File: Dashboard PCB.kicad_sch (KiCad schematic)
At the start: 38 parts

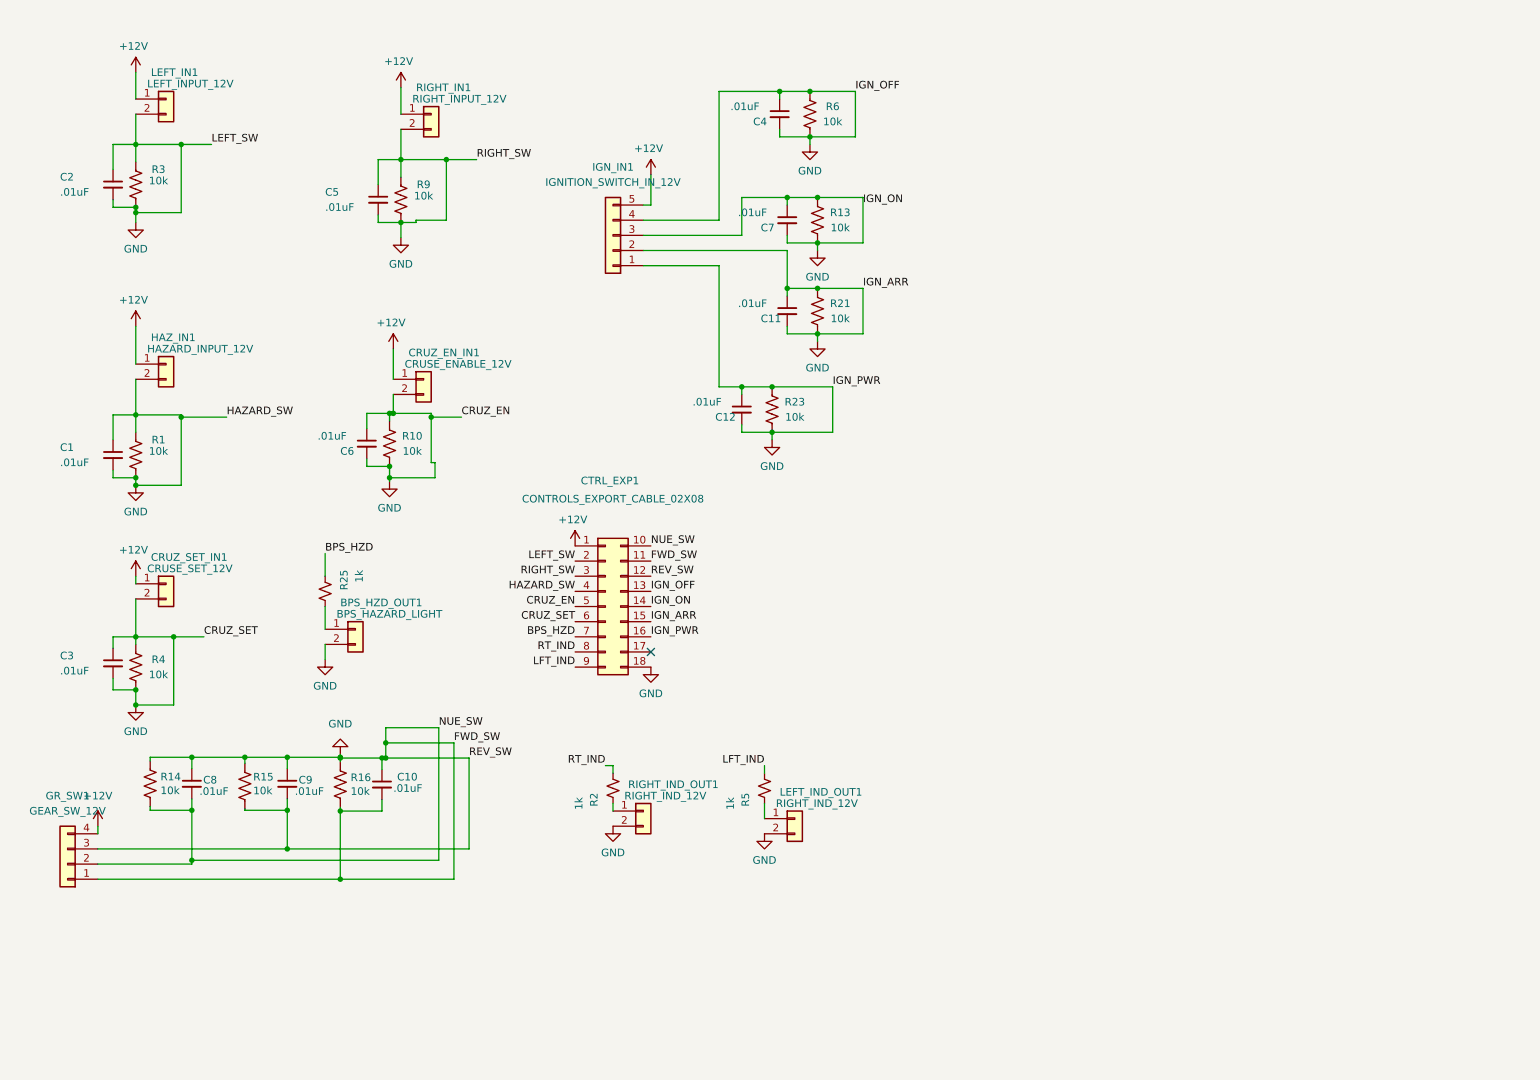
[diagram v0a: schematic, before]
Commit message: Ready for review I think :+1:
Switched design from modular to big board :). Plz rev schem thaks :P
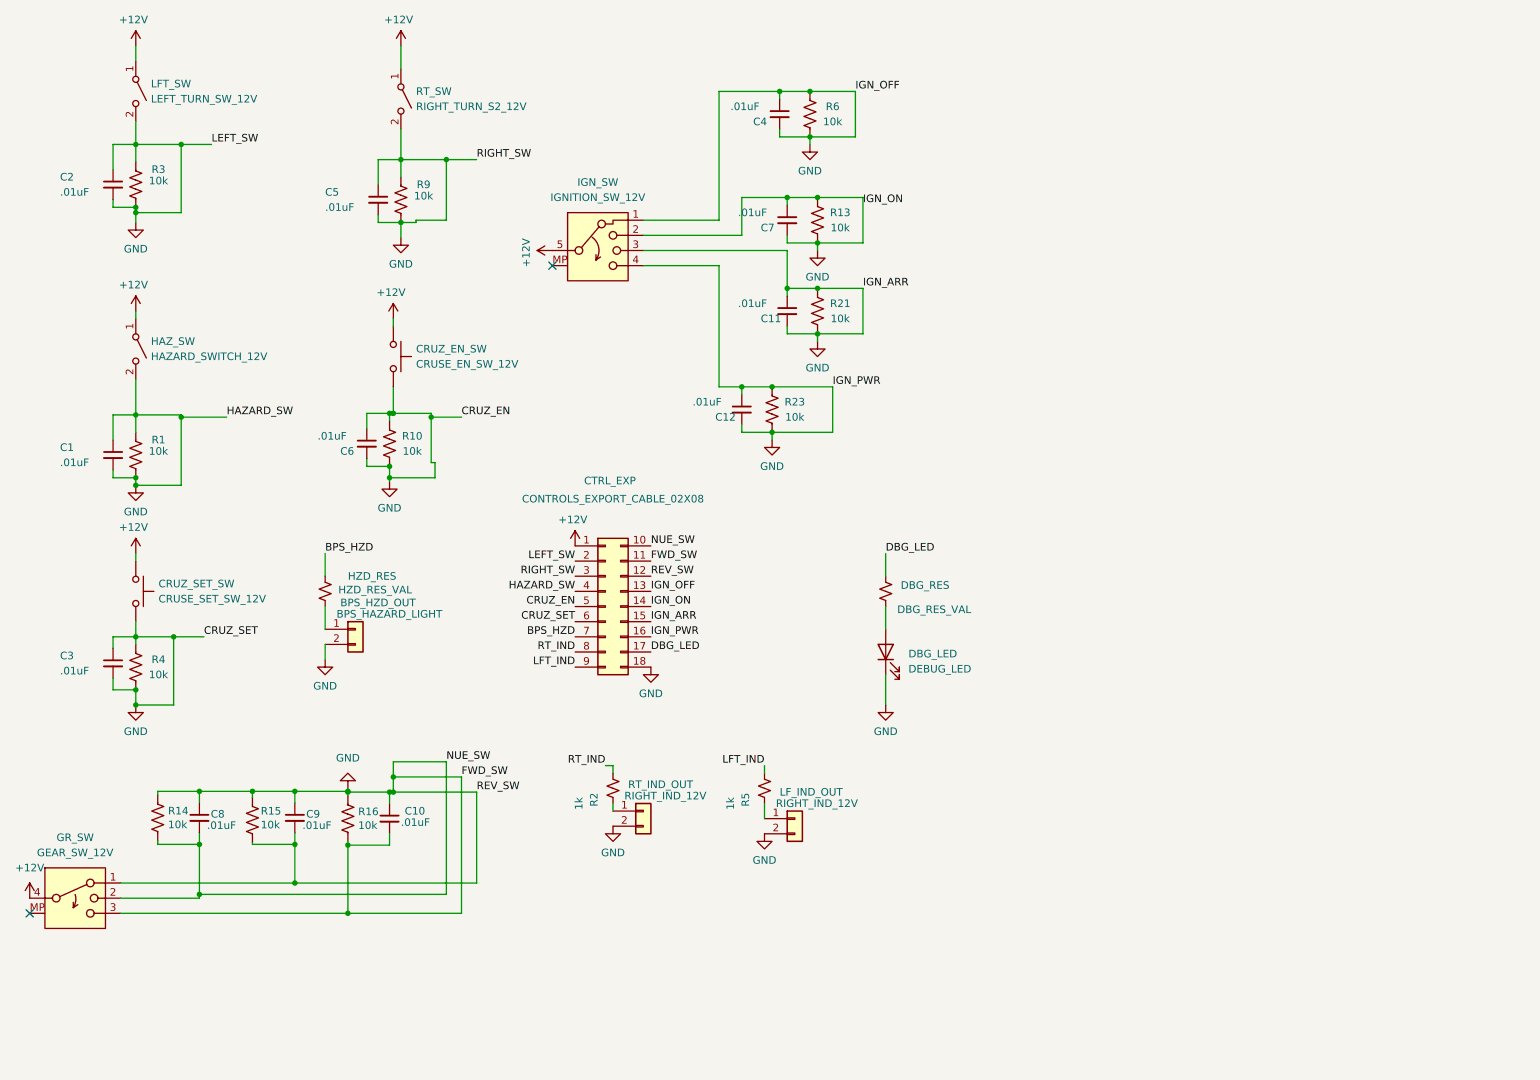
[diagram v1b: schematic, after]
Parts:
- removed CRUZ_EN_IN1: CRUSE_ENABLE_12V, Connector_Molex:Molex_Micro-Fit_3.0_43650-0215_1x02_P3.00mm_Vertical, symbol Connector_Generic:Conn_01x02
- removed CRUZ_SET_IN1: CRUSE_SET_12V, Connector_Molex:Molex_Micro-Fit_3.0_43650-0215_1x02_P3.00mm_Vertical, symbol Connector_Generic:Conn_01x02
- removed GR_SW1: GEAR_SW_12V, symbol Connector_Generic:Conn_01x04
- removed HAZ_IN1: HAZARD_INPUT_12V, Connector_Molex:Molex_Micro-Fit_3.0_43650-0215_1x02_P3.00mm_Vertical, symbol Connector_Generic:Conn_01x02
- removed IGN_IN1: IGNITION_SWITCH_IN_12V, symbol Connector_Generic:Conn_01x05
- removed LEFT_IN1: LEFT_INPUT_12V, Connector_Molex:Molex_Micro-Fit_3.0_43650-0215_1x02_P3.00mm_Vertical, symbol Connector_Generic:Conn_01x02
- removed RIGHT_IN1: RIGHT_INPUT_12V, Connector_Molex:Molex_Micro-Fit_3.0_43650-0215_1x02_P3.00mm_Vertical, symbol Connector_Generic:Conn_01x02
- added CRUZ_EN_SW: CRUSE_EN_SW_12V, symbol Switch:SW_Push
- added CRUZ_SET_SW: CRUSE_SET_SW_12V, symbol Switch:SW_Push
- added DBG_LED: DEBUG_LED, symbol Device:LED
- added DBG_RES: DBG_RES_VAL, Resistor_SMD:R_0805_2012Metric, symbol Device:R_Small_US
- added GR_SW: GEAR_SW_12V, symbol Switch:SW_Rotary_1x3_MP
- added HAZ_SW: HAZARD_SWITCH_12V, symbol Switch:SW_SPST
- added IGN_SW: IGNITION_SW_12V, symbol Switch:SW_Rotary_1x4_MP
- added LFT_SW: LEFT_TURN_SW_12V, symbol Switch:SW_SPST
- added RT_SW: RIGHT_TURN_S2_12V, symbol Switch:SW_SPST
- HZD_RES: renamed from R25; value 1k -> HZD_RES_VAL
- renumbered BPS_HZD_OUT1 to BPS_HZD_OUT, CTRL_EXP1 to CTRL_EXP, LEFT_IND_OUT1 to LF_IND_OUT, RIGHT_IND_OUT1 to RT_IND_OUT
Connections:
- net +12V: now also CRUZ_EN_SW.1, CRUZ_SET_SW.1, GR_SW.4, HAZ_SW.1 (A), IGN_SW.5, LFT_SW.1 (A), RT_SW.1 (A)
- net GND: now also CRUZ_EN_SW.2, CRUZ_SET_SW.2, DBG_LED.1 (K), GR_SW.1, GR_SW.2, GR_SW.3, HAZ_SW.2 (B), IGN_SW.1, IGN_SW.2, IGN_SW.3, IGN_SW.4, LFT_SW.2 (B), RT_SW.2 (B)
- net DBG_LED: now reaches CTRL_EXP.17 (Pin_17)
- net DBG_LED: now also DBG_RES.1
- new net: DBG_LED.2 (A), DBG_RES.2
- no-connect marks 1 -> 2
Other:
- moved on the sheet: C10, C8, C9, R14, R15, R16

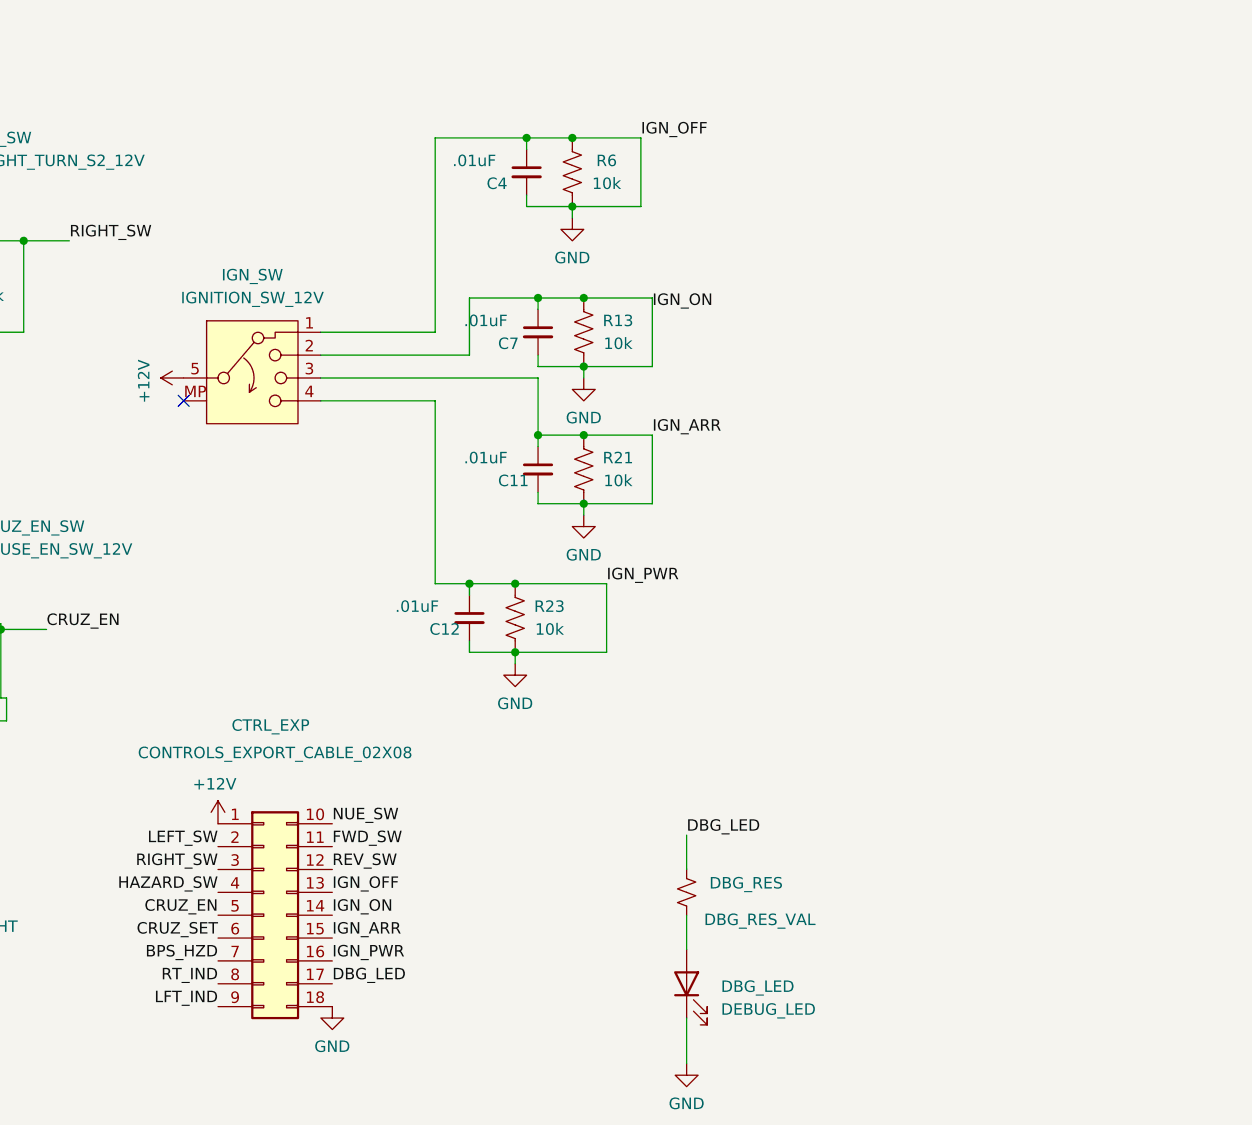
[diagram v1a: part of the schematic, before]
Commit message: Hotfix
Changed ignition switch to not have ON, and added supp pwr switch
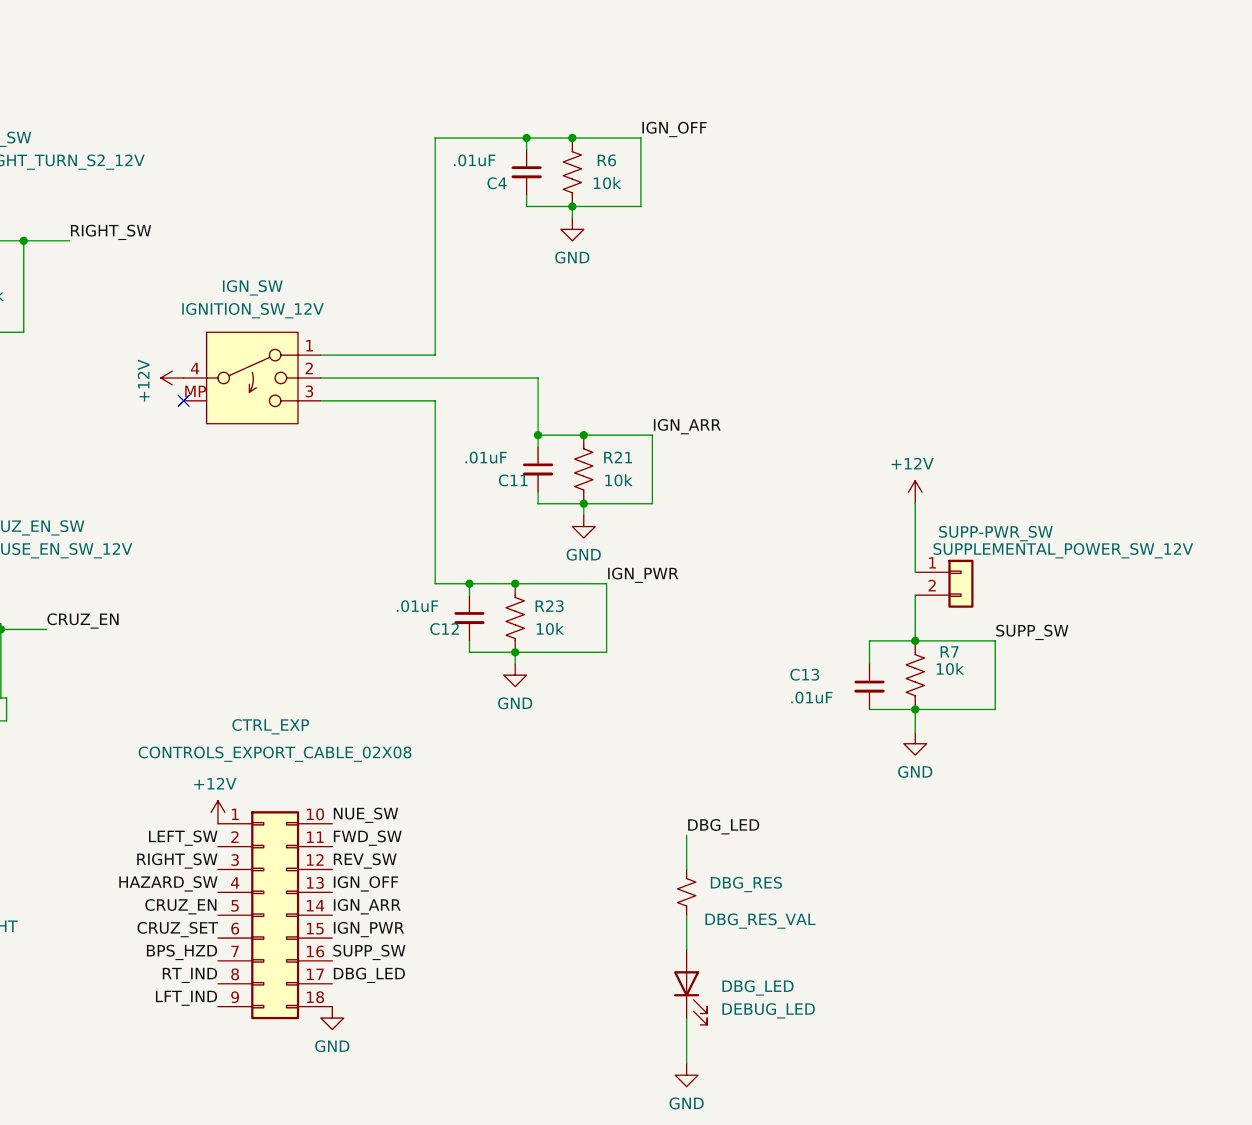
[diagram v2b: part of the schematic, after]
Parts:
- removed C7: .01uF, Capacitor_SMD:C_0805_2012Metric, symbol Device:C_Small
- removed IGN_SW: IGNITION_SW_12V, symbol Switch:SW_Rotary_1x4_MP
- removed R13: 10k, Resistor_SMD:R_0805_2012Metric, symbol Device:R_US
- added C13: .01uF, Capacitor_SMD:C_0805_2012Metric, symbol Device:C_Small
- added IGN_SW: IGNITION_SW_12V, symbol Switch:SW_Rotary_1x3_MP
- added R7: 10k, Resistor_SMD:R_0805_2012Metric, symbol Device:R_US
- added SUPP-PWR_SW: SUPPLEMENTAL_POWER_SW_12V, Connector_Molex:Molex_Micro-Fit_3.0_43650-0215_1x02_P3.00mm_Vertical, symbol Connector_Generic:Conn_01x02
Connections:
- net +12V: now also IGN_SW.4, SUPP-PWR_SW.1 (Pin_1)
- net GND: now also C13.1, C13.2, IGN_SW.1, IGN_SW.2, IGN_SW.3, R7.1, R7.2, SUPP-PWR_SW.2 (Pin_2)

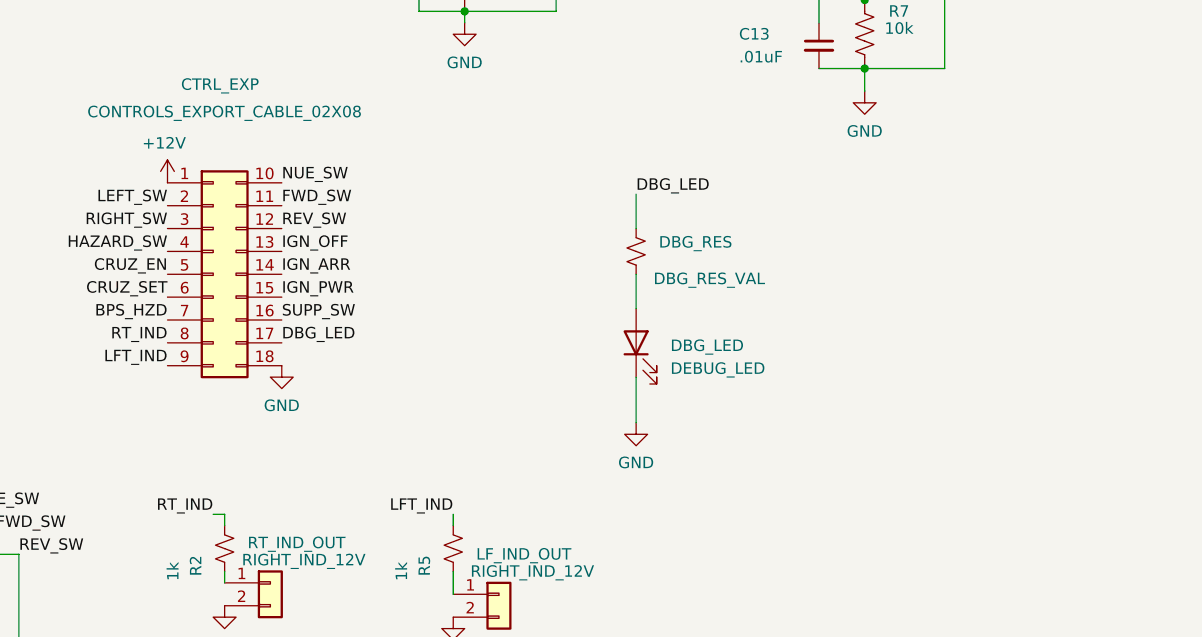
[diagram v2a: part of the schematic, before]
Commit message: Added dashboard fan connection
Not sure if i need to do anything specific with the fan (flyback diode?)
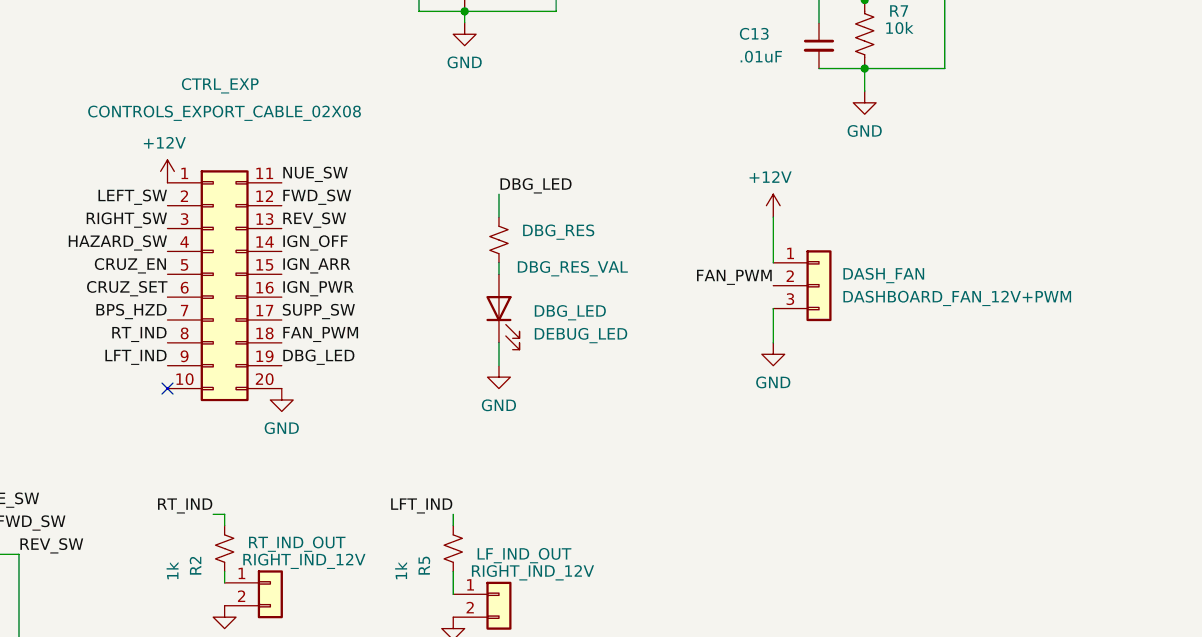
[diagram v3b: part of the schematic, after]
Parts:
- added DASH_FAN: DASHBOARD_FAN_12V+PWM, symbol Connector_Generic:Conn_01x03
- CTRL_EXP: symbol Connector_Generic:Conn_02x09_Top_Bottom -> Connector_Generic:Conn_02x10_Top_Bottom
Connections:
- net +12V: now also DASH_FAN.1 (Pin_1)
- net DBG_LED: now also CTRL_EXP.19 (Pin_19); no longer CTRL_EXP.17 (Pin_17)
- net GND: now also CTRL_EXP.17 (Pin_17), CTRL_EXP.20 (Pin_20), DASH_FAN.3 (Pin_3); no longer CTRL_EXP.10 (Pin_10), CTRL_EXP.18 (Pin_18)
- new net FAN_PWM: CTRL_EXP.18 (Pin_18), DASH_FAN.2 (Pin_2)
- no-connect marks 2 -> 3
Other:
- moved on the sheet: DBG_LED, DBG_RES
